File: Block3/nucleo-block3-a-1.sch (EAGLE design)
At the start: 51 parts, among them J4 MODJACK-6P6CCONN_SS-90000-003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, J5 MODJACK-6P6CCONN_SS-90000-003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, Q1 NPN-23, Q2 BSS84, U1 TC4428ACOA, U2 TC4428ACOA, U3 TC4428ACOA

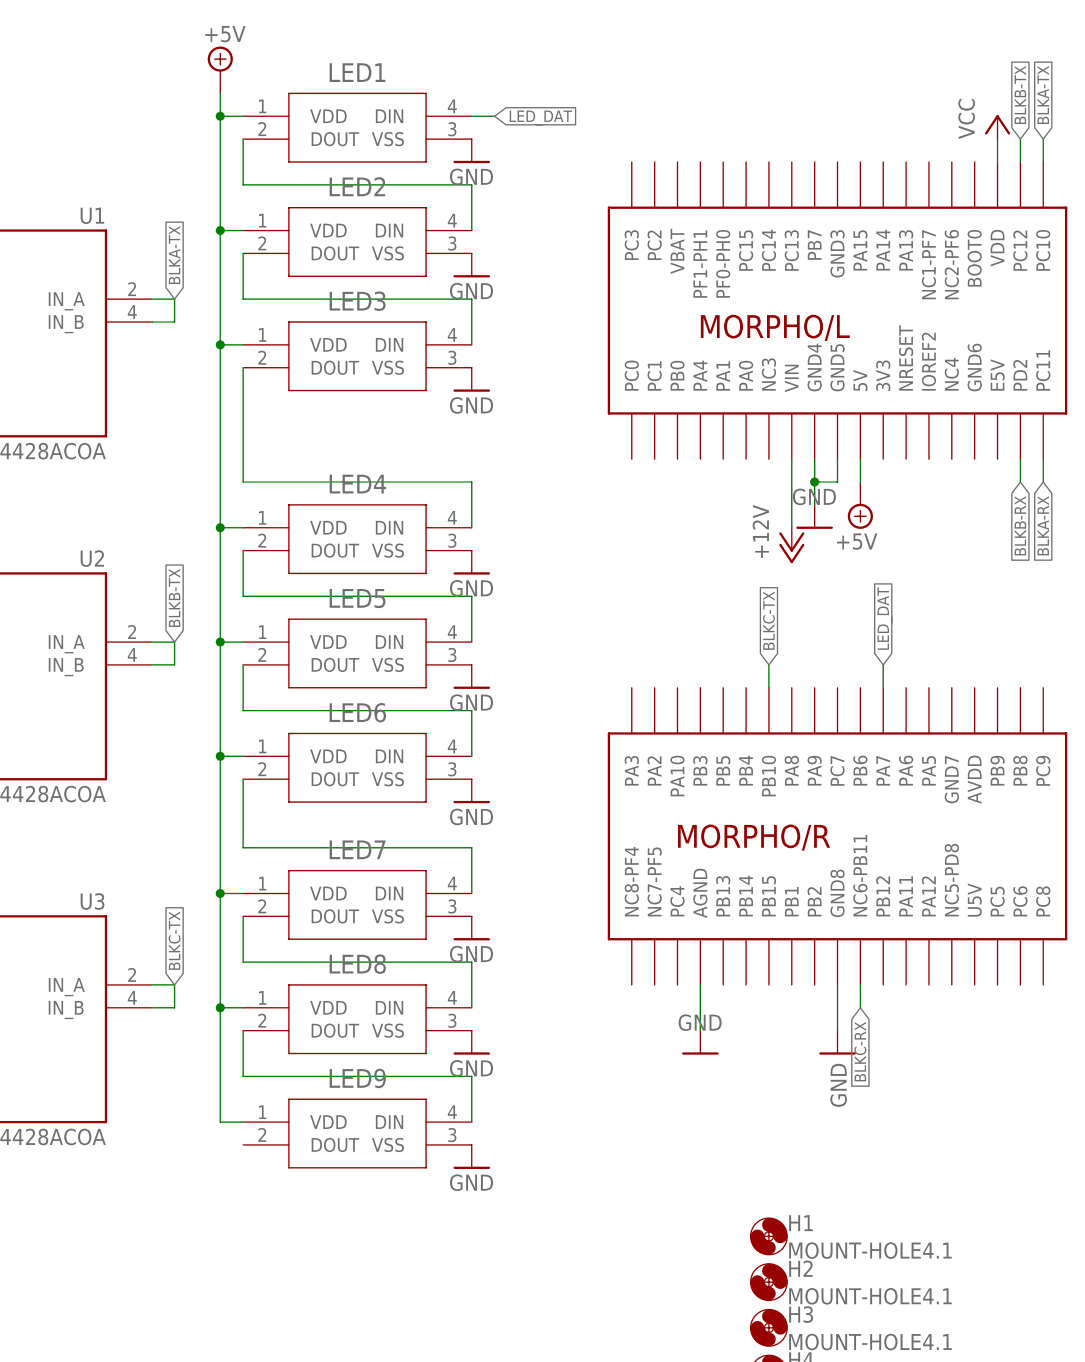
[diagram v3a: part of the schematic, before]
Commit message: Replace 6p6c jack with a different one that is smaller in size.
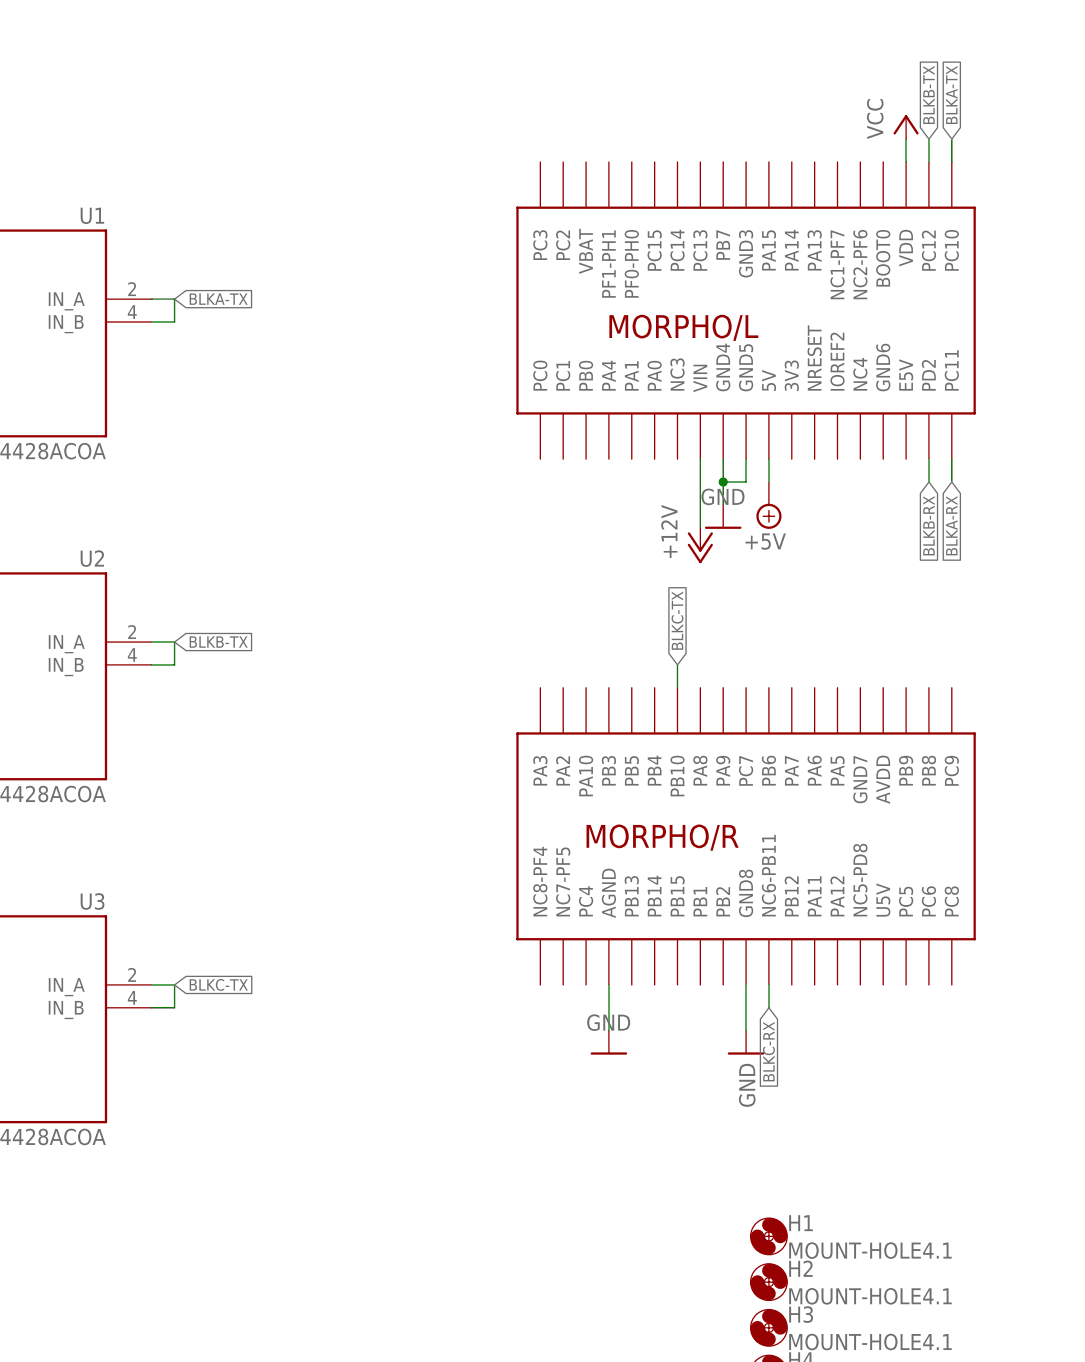
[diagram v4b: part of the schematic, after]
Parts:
- removed LED1, LED2, LED3, LED4, LED5, LED6, LED7, LED8, LED9: LED-2812BCOM-16347_SPK-M, eagleparts:LED-2812BCOM-16347_SPK-M
- J4, J5: value MODJACK-6P6CCONN_SS-90000-003_STW -> MODJACK6P6C-MJ3245-66-0CONN_MJ3245-66-0_GCT; device eagleparts:MODJACK-6P6CCONN_SS-90000-003_STW -> eagleparts:MODJACK6P6C-MJ3245-66-0CONN_MJ3245-66-0_GCT
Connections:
- removed net LED_DAT: G1.PA7, LED1.DIN
- removed net N$12: LED1.DOUT, LED2.DIN
- removed net N$13: LED2.DOUT, LED3.DIN
- removed net N$14: LED3.DOUT, LED4.DIN
- removed net N$15: LED4.DOUT, LED5.DIN
- removed net N$16: LED5.DOUT, LED6.DIN
- removed net N$17: LED6.DOUT, LED7.DIN
- removed net N$18: LED7.DOUT, LED8.DIN
- removed net N$19: LED8.DOUT, LED9.DIN
- net +5V: no longer LED1.VDD, LED2.VDD, LED3.VDD, LED4.VDD, LED5.VDD, LED6.VDD, LED7.VDD, LED8.VDD, LED9.VDD
- net GND: no longer LED1.VSS, LED2.VSS, LED3.VSS, LED4.VSS, LED5.VSS, LED6.VSS, LED7.VSS, LED8.VSS, LED9.VSS
